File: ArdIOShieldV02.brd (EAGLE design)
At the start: 100 x 80 mm, 30 parts

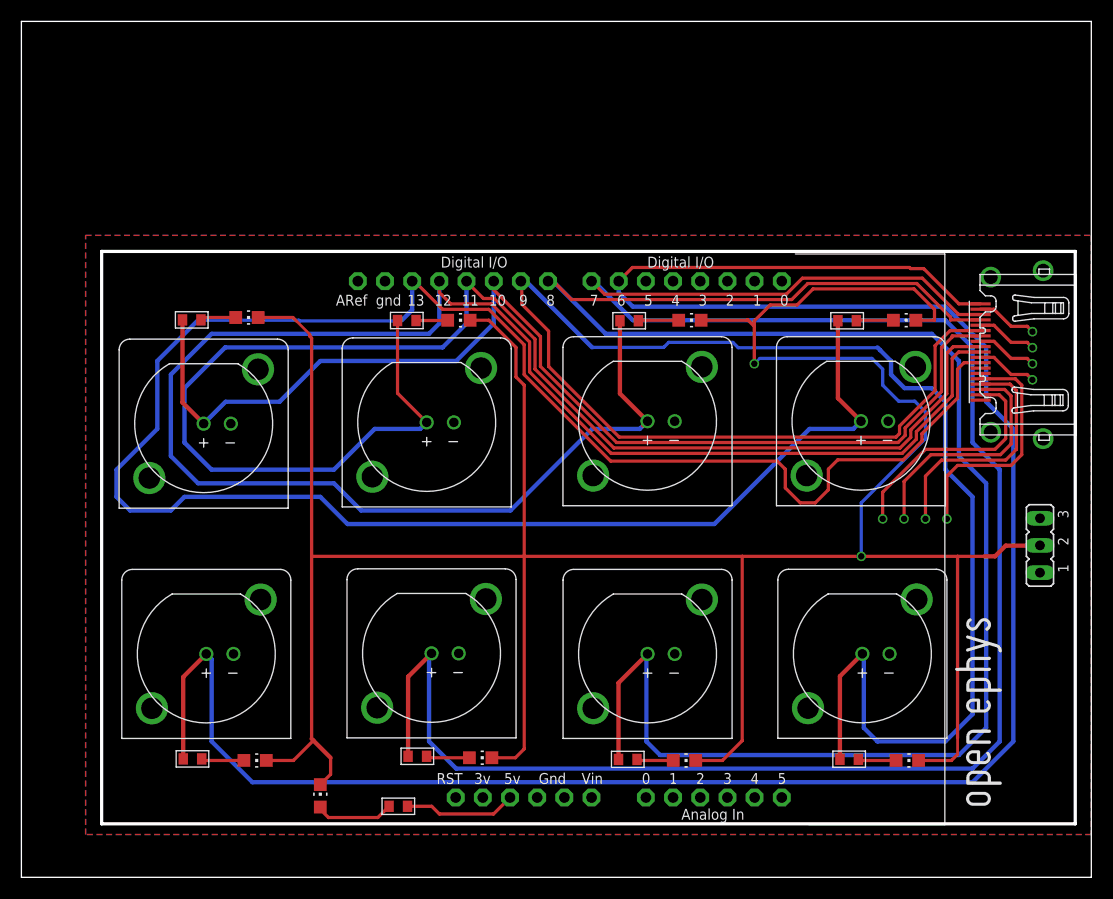
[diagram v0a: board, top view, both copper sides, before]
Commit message: USB overlap fixed
Shifted holes for arduino so board no longer rests on USB.
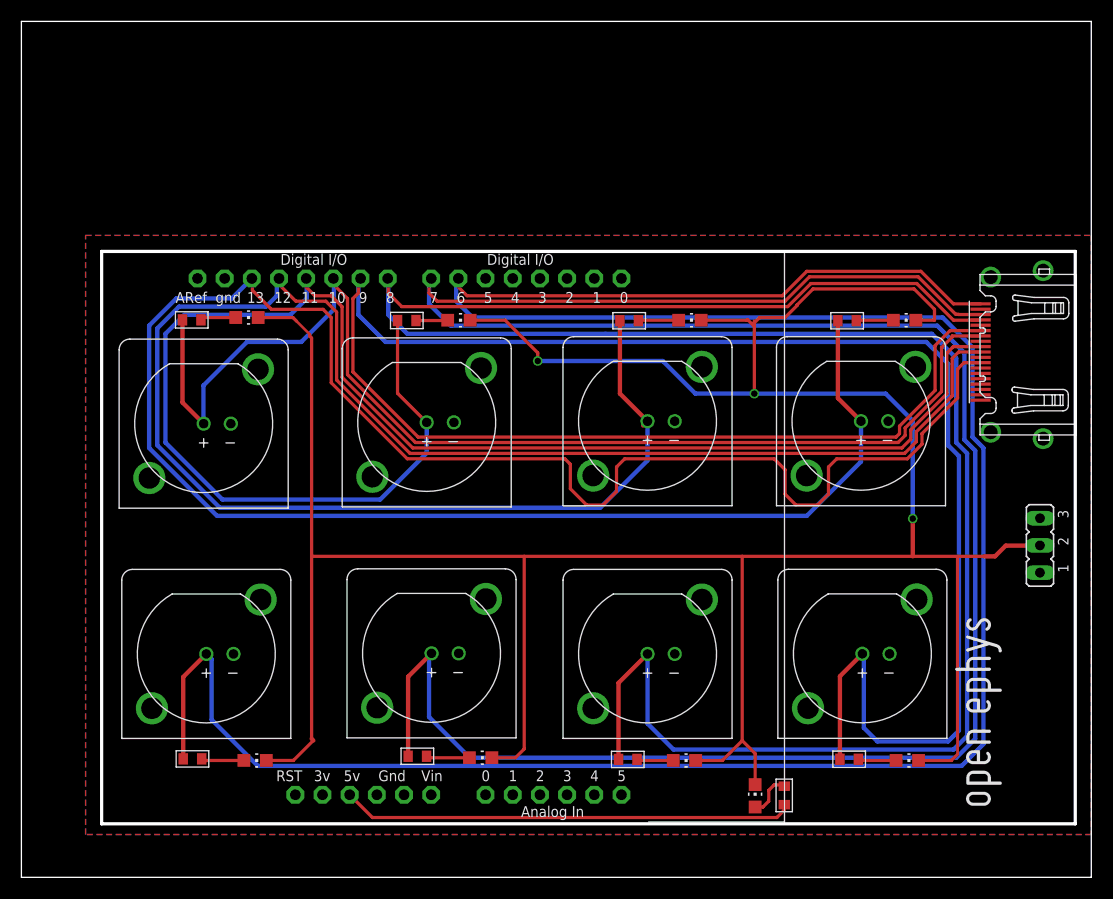
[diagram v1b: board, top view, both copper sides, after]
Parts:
- moved LED17 40.6 mm to (68.6, 7.62)
- moved R4 36.1 mm to (71.3, 7.66), turned to 270 degrees
- moved U$1 15.0 mm to (-7.42, 5.17)
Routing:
- net GND: track 112.7 -> 0.00 mm, vias 8 -> 0
- net D9: track 164.6 -> 199.9 mm
- net N$2: track 10.5 -> 42.3 mm
- net D8: track 172.7 -> 202.4 mm
- net D7: track 189.3 -> 216.5 mm
- net D6: track 208.3 -> 233.7 mm
- net D11: track 136.8 -> 149.2 mm
- net D12: track 165.7 -> 172.7 mm
- net D13: track 201.7 -> 206.0 mm
- net D10: track 106.3 -> 110.5 mm
- net N$3: track 7.59 -> 4.22 mm
- net LED: track 279.7 -> 280.2 mm, vias 2 -> 3
